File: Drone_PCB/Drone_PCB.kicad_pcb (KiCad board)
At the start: 2 copper layers, 76 x 51 mm, 63 parts, among them J1 Conn_01x04_Pin, J2 Conn_01x08_Socket, J3 Conn_01x05_Socket, J4 Conn_01x02_Socket, J5 Conn_01x02_Socket, J6 Conn_01x02_Socket, J7 Conn_01x02_Socket, J8 Conn_01x02_Socket, J9 USB_B_Micro, Q1 AO3400A, Q2 AO3400A, Q3 AO3400A, Q4 AO3400A, Q5 AO3400A, Q6 AO3400A, SW1 SW_Push, SW2 SW_SPST, U1 STM32F411RCT6, U2 AP2112K-3.3, U3 TP4056-42-ESOP8, U4 DW01A, Y1 26MHz

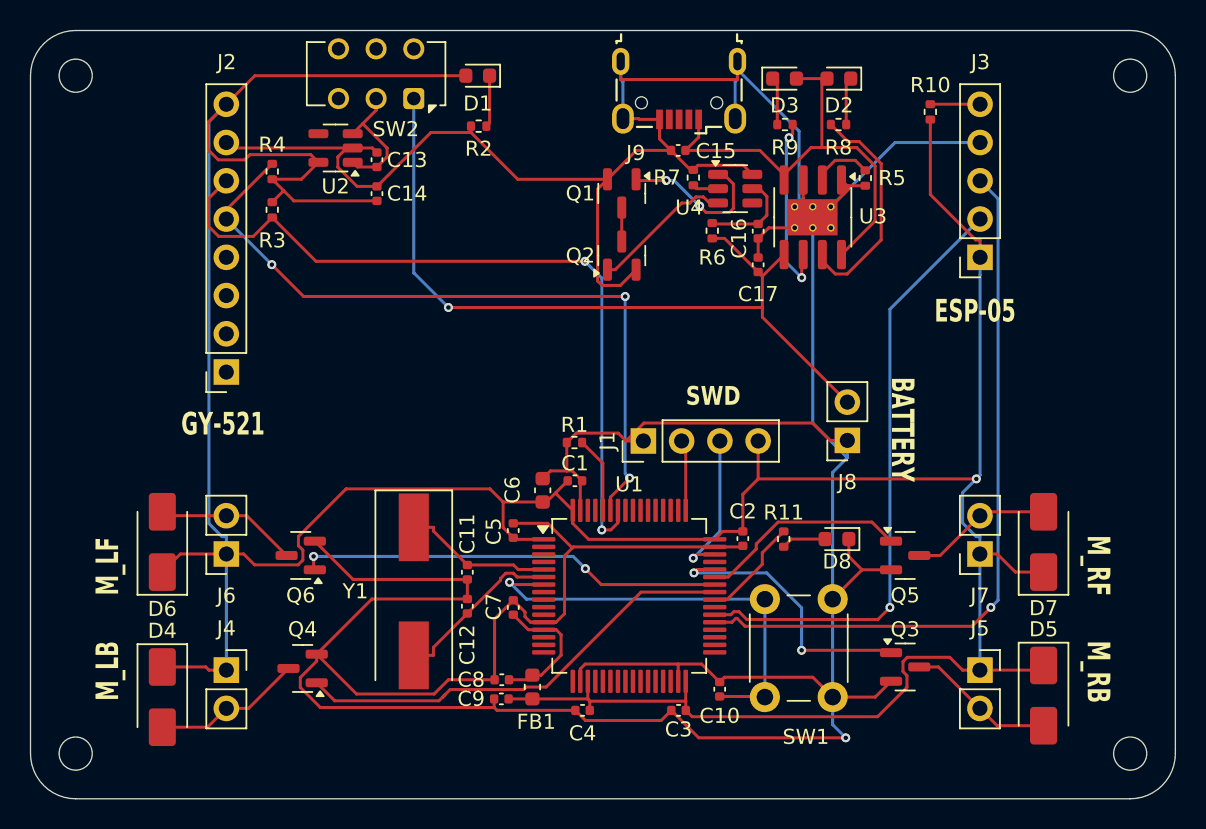
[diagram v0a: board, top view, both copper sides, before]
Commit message: Changed schematic
FreeRouting does kinda lame job. Removed routes and moved some elements
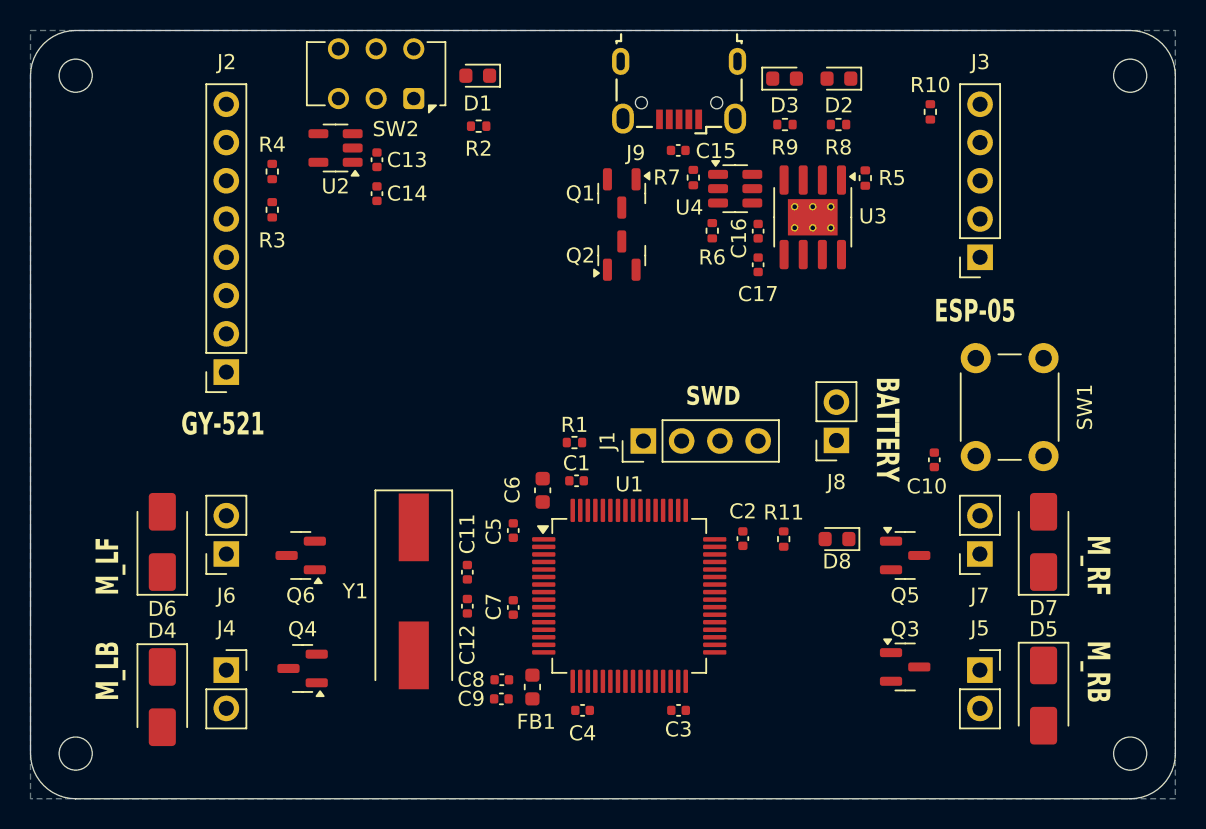
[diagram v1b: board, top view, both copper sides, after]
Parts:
- moved SW1 21.3 mm to (97.2, 80.2)
- moved C10 20.9 mm to (94.5, 80.5)
- moved J8 0.72 mm to (88.0, 79.2)
- moved C1 0.11 mm to (70.8, 81.9)
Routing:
- net GND: track 322.7 -> 0.00 mm, vias 1 -> 0
- net +3.3V: track 242.3 -> 0.00 mm, vias 1 -> 0
- net /B+: track 52.8 -> 0.00 mm, vias 1 -> 0
- net /SCL: track 50.9 -> 0.00 mm, vias 2 -> 0
- net /SDA: track 48.4 -> 0.00 mm, vias 3 -> 0
- net /RX: track 48.2 -> 0.00 mm, vias 1 -> 0
- net /TX: track 40.5 -> 0.00 mm, vias 1 -> 0
- net VBUS: track 30.7 -> 0.00 mm
- net /PWM_LB: track 30.1 -> 0.00 mm
- net /NRST: track 29.3 -> 0.00 mm, vias 1 -> 0
- net /PWM_LF: track 28.3 -> 0.00 mm, vias 2 -> 0
- net /PWM_RB: track 18.4 -> 0.00 mm, vias 2 -> 0
- net /CHRG_LED: track 15.1 -> 0.00 mm
- net /PWM_RF: track 13.9 -> 0.00 mm
- net /STDBY_LED: track 12.3 -> 0.00 mm, vias 2 -> 0
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- added copper zone on B.Cu, net GND

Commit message: Added GND routes
It should work okay now
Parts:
- moved U3 20.6 mm to (67.3, 72.3)
- moved Q1 15.7 mm to (59.0, 68.3)
- moved Q2 15.7 mm to (59.0, 72.4)
- moved R6 15.0 mm to (64.8, 64.2)
- moved U4 13.9 mm to (67.9, 66.3)
- moved R7 10.2 mm to (68.5, 63.8), turned to 0 degrees
- moved C17 9.93 mm to (74.2, 62.5), turned to 0 degrees
- moved C16 8.56 mm to (74.2, 65.5), turned to 0 degrees
- moved C15 2.73 mm to (78.5, 62.5)
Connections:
- C13 pad 1: /PWR -> PWR
- D4 pad 1: +3.3V -> PWR
- D5 pad 1: +3.3V -> PWR
- D6 pad 1: +3.3V -> PWR
- D7 pad 1: +3.3V -> PWR
- J4 pad 1: +3.3V -> PWR
- J5 pad 1: +3.3V -> PWR
- J6 pad 1: +3.3V -> PWR
- J7 pad 1: +3.3V -> PWR
- SW2 pad 2: /PWR -> PWR
- U2 pad 1: /PWR -> PWR
- U2 pad 3: /PWR -> PWR
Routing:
- net GND: track 0.00 -> 30.6 mm
- net +3.3V: track 0.00 -> 12.1 mm
- net +3.3VA: track 0.00 -> 7.46 mm
- added copper zone on F.Cu, net GND
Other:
- copper layers 2 -> 4

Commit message: Made the rest of routes-ish
Sort of
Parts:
- moved R5 19.7 mm to (71.4, 68.6)
- moved R3 2.61 mm to (50.3, 61.3)
- moved R4 2.55 mm to (50.3, 63.9)
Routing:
- net +3.3V: track 12.1 -> 76.2 mm
- net VBUS: track 0.00 -> 39.5 mm
- net PWR: track 0.00 -> 36.2 mm
- net GND: track 30.6 -> 44.2 mm
- net /M_RB: track 0.00 -> 11.5 mm
- net /M_LB: track 0.00 -> 11.3 mm
- net /HSE_IN: track 0.00 -> 11.2 mm
- net /M_RF: track 0.00 -> 11.0 mm
- net /M_LF: track 0.00 -> 10.7 mm
- net /B+: track 0.00 -> 9.96 mm
- net /SWDIO: track 0.00 -> 9.55 mm
- net /HSE_OUT: track 0.00 -> 6.29 mm
- net /VIN: track 0.00 -> 5.08 mm
- net /PROG: track 0.00 -> 4.81 mm
- net /SWCLK: track 0.00 -> 4.72 mm
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
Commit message: Full routing
Man, that was hard
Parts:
- moved U3 17.5 mm to (84.0, 66.9), turned to 0 degrees
- moved C10 10.1 mm to (103.9, 76.9)
- moved R5 8.11 mm to (79.3, 66.9)
- moved R6 7.00 mm to (71.6, 65.8), turned to 90 degrees
- moved R10 6.47 mm to (100.7, 57.4)
- moved R4 5.68 mm to (44.6, 64.0), turned to -90 degrees
- moved R8 4.69 mm to (83.5, 58.7), turned to -90 degrees
- moved C14 4.46 mm to (53.6, 65.0), turned to -90 degrees
- moved D8 4.32 mm to (86.5, 89.8)
- moved R11 4.09 mm to (83.7, 89.8), turned to 180 degrees
- moved D2 3.89 mm to (84.3, 55.2), turned to 0 degrees
- moved C12 3.53 mm to (66.8, 89.0), turned to -90 degrees
- moved C11 3.46 mm to (66.8, 87.0), turned to 90 degrees
- moved D3 2.93 mm to (87.5, 55.2)
- moved J1 2.92 mm to (76.6, 76.7)
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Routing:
- net PWR: track 36.2 -> 183.5 mm, vias 0 -> 10
- net +3.3V: track 76.2 -> 174.6 mm, vias 0 -> 12
- net /NRST: track 3.05 -> 58.0 mm
- net /TX: track 0.00 -> 49.3 mm
- net /PWM_LF: track 0.00 -> 48.4 mm, vias 0 -> 4
- net /RX: track 0.00 -> 45.2 mm
- net /B+: track 9.96 -> 55.2 mm
- net /SCL: track 2.87 -> 45.2 mm
- net /PWM_LB: track 0.00 -> 40.7 mm, vias 0 -> 4
- net /SDA: track 3.27 -> 43.9 mm
- net /PWM_RB: track 0.00 -> 24.3 mm, vias 0 -> 2
- net /OC: track 0.00 -> 18.1 mm
- net /PWM_RF: track 0.00 -> 16.0 mm, vias 0 -> 2
- net /CHRG_LED: track 0.00 -> 12.4 mm
- net /STDBY_LED: track 0.00 -> 11.5 mm
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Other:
- copper layers 4 -> 2

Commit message: Final routes
I guess it's okay now
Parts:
- Y1: footprint Crystal:Crystal_SMD_HC49-SD -> Crystal:Crystal_SMD_3225-4Pin_3.2x2.5mm
- moved Y1 2.30 mm to (64.2, 87.6)
- moved C5 2.24 mm to (64.8, 83.3), turned to 180 degrees
- moved C11 0.66 mm to (66.5, 86.4)
- moved C12 0.40 mm to (66.5, 88.8)
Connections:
- Y1 pad 2: /HSE_OUT -> GND
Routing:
- net GND: track 49.5 -> 58.2 mm
- net /HSE_OUT: track 10.3 -> 3.68 mm
- net /HSE_IN: track 9.97 -> 6.29 mm
- net +3.3V: track 174.6 -> 175.4 mm
